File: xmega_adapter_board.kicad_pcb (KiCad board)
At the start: 2 copper layers, 31 x 72.4 mm, 17 parts, among them J1 Conn_01x04, J2 Conn_01x08, J3 Conn_01x08, J4 Conn_01x04, J5 Conn_01x08, J6 Conn_01x08, J7 Conn_01x08, J8 Conn_01x08, U1 ATxmega256D3-AU

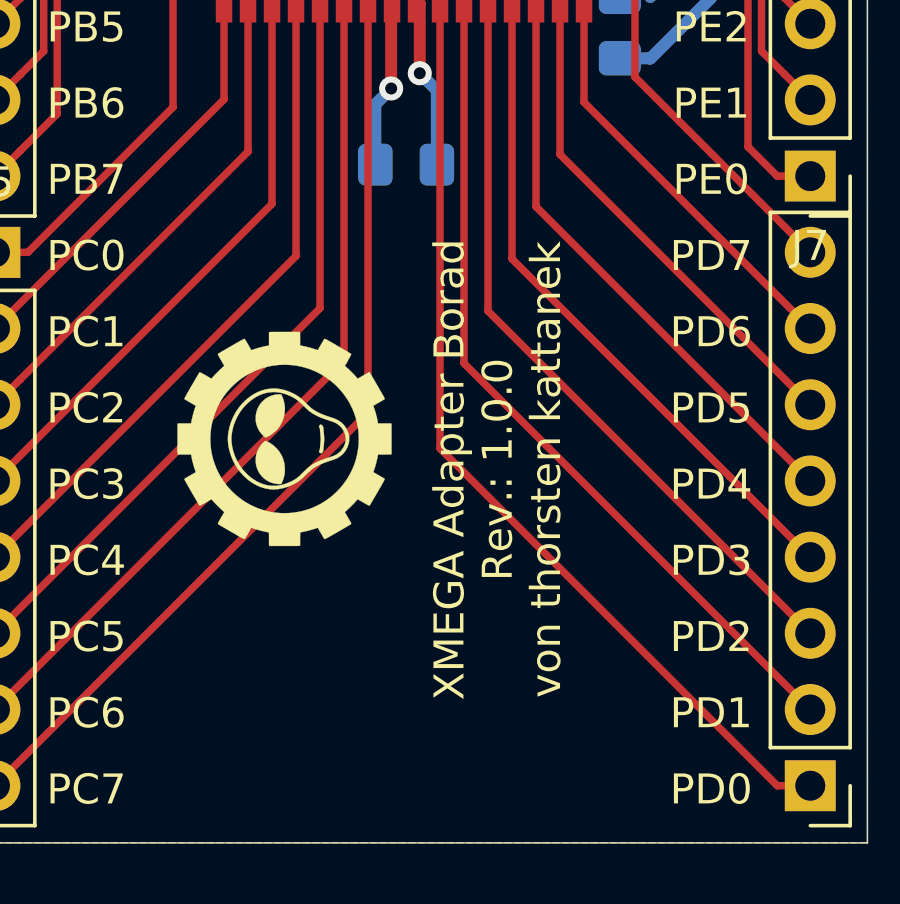
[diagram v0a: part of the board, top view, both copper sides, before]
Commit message: Beschriftung geaendert, borad -> board
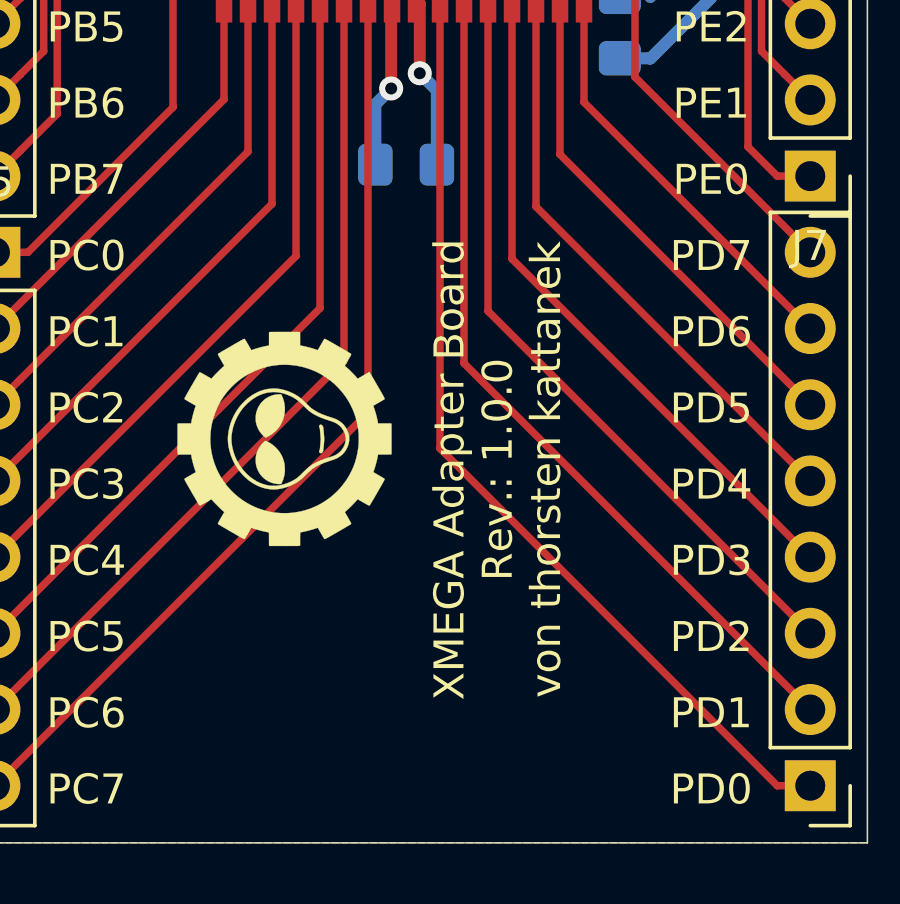
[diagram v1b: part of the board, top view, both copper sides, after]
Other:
- board text added: "XMEGA Adapter Board Rev.: 1.0.0 von thorsten kattanek"
- board text removed: "XMEGA Adapter Borad Rev.: 1.0.0 von thorsten kattanek"
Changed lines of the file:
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@@
     (effects (font (size 1 1) (thickness 0.15)) (justify mirror))
   )
-  (gr_text "XMEGA Adapter Borad\nRev.: 1.0.0\nvon thorsten kattanek" (at 204.724 124.46 90) (layer F.SilkS)
+  (gr_text "XMEGA Adapter Board\nRev.: 1.0.0\nvon thorsten kattanek" (at 204.724 124.46 90) (layer F.SilkS)
     (effects (font (size 1 1) (thickness 0.15)))
   )
